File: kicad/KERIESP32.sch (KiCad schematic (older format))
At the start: 18 parts, among them J1 ZX62R-B-5P, P1 CONN, SW1 RESET, SW2 IO0, U1 ESP-WROOM-32, U2 NJM2884, U3 FT231XS

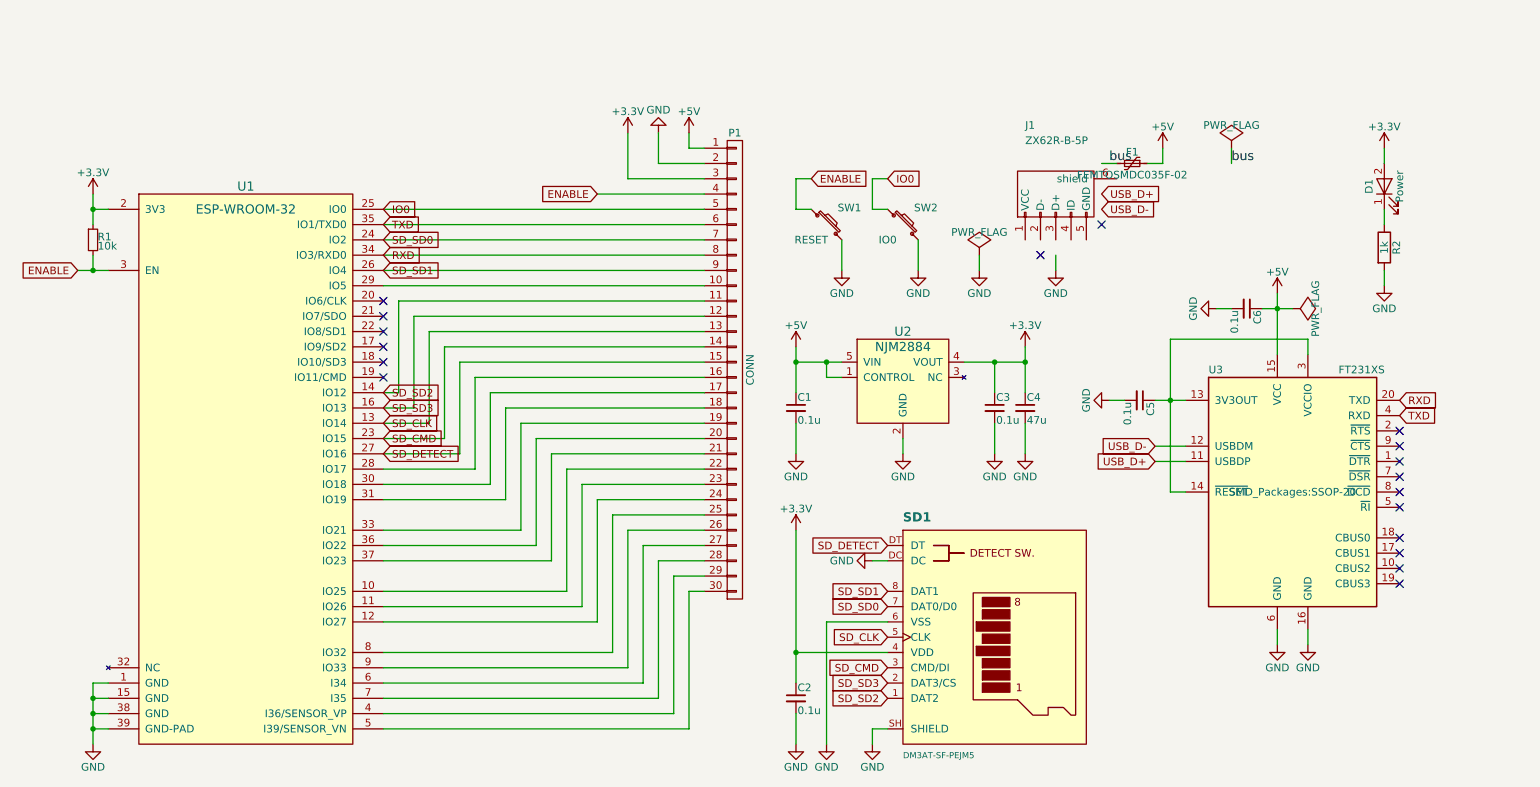
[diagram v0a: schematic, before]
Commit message: 回路図を整理
PDFを出力
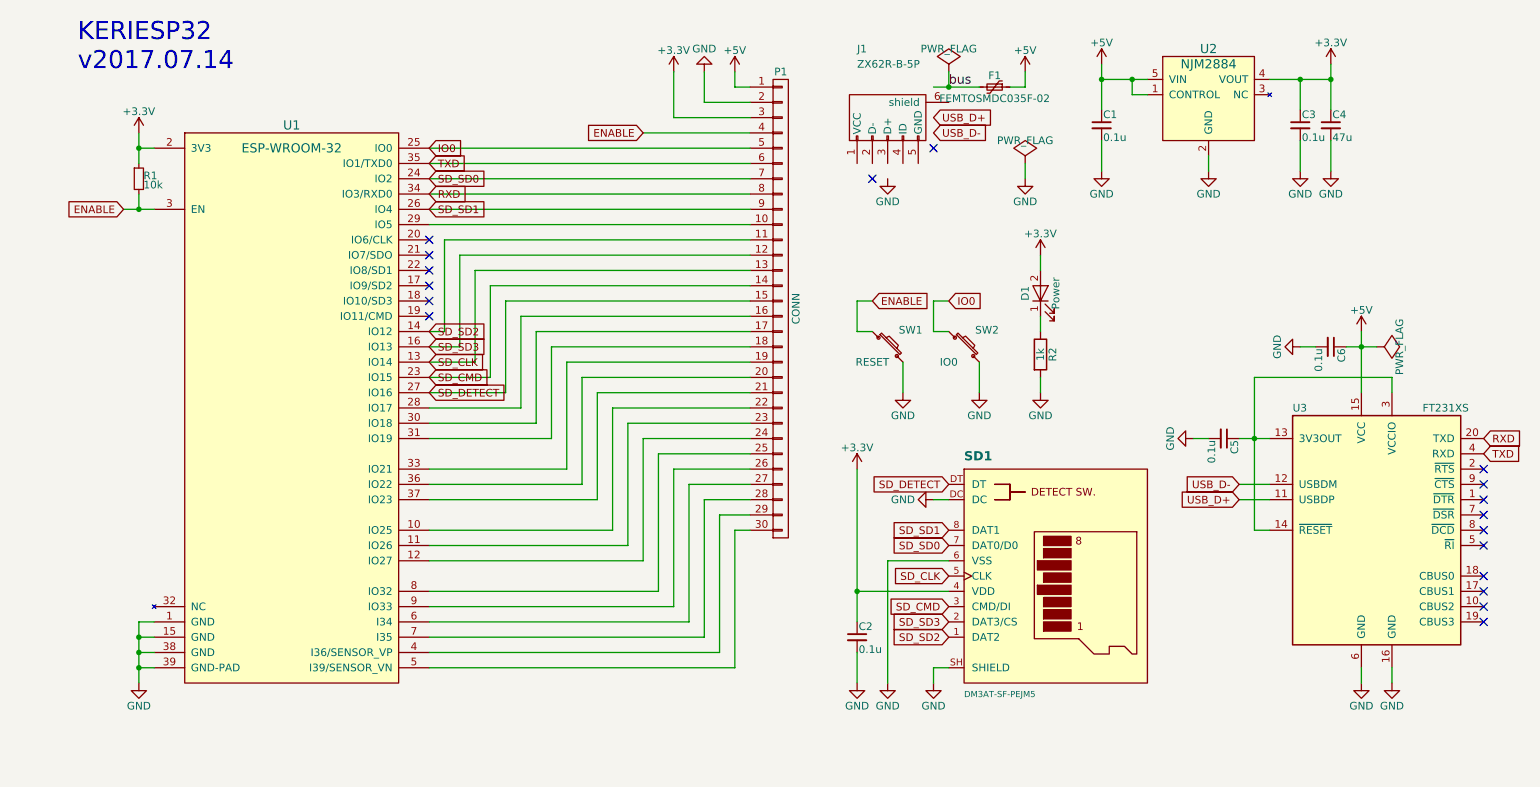
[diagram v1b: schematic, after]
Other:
- note added: "KERIESP32\nv2017.07.14"
- moved on the sheet: C1, C2, C3, C4, C5, C6, D1, F1, J1, P1, R1, R2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
